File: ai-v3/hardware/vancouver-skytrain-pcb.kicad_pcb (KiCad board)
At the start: 2 copper layers, 200 x 109 mm, 90 parts, among them SW1 TS-1187A-B-A-B, SW2 TS-1187A-B-A-B, SW3 TS-1187A-B-A-B, SW4 TS-1187A-B-A-B, U1 XIAO-RP2040-DIP

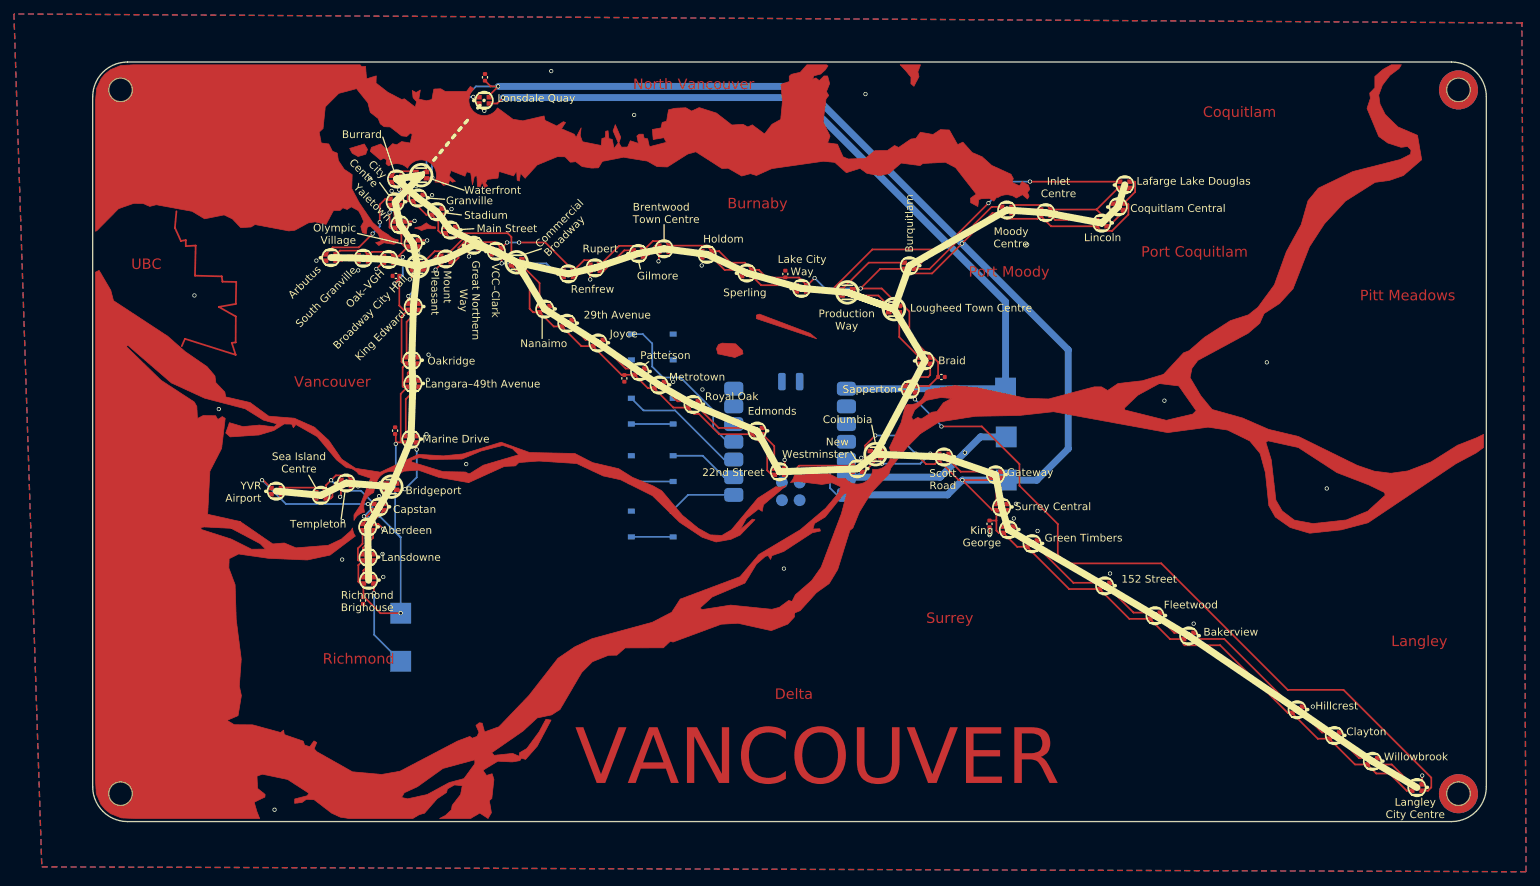
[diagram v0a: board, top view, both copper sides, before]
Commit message: ai-v3: JLCPCB fabrication outputs
hardware/jlcpcb/: gerbers (9 layers, Protel extensions, mask-subtracted
silk) + Excellon drill and map zipped for the order page; BOM and CPL in
JLC's column format for SMT assembly, covering the 68 WS2812B LEDs
(C5349954) and 8 x 10uF 0402 (C52923) - switches are DNP, the XIAO is a
hand-soldered module. tools/make_jlcpcb.py derives the two JLC files
from kicad-cli's raw pos/BOM exports and builds the zip; README.md in
the folder has the upload map and the exact commands.

DRC at this state (KiCad 10.0.5): no unconnected items, no clearance /
edge / courtyard violations; remaining are the two no-net mounting holes
touching the water copper and two thin GND thermals (LED35, LED38).
Includes the user's +5V and GND zone routing fixes.

Co-Authored-By: Claude Fable 5.1 <noreply@anthropic.com>
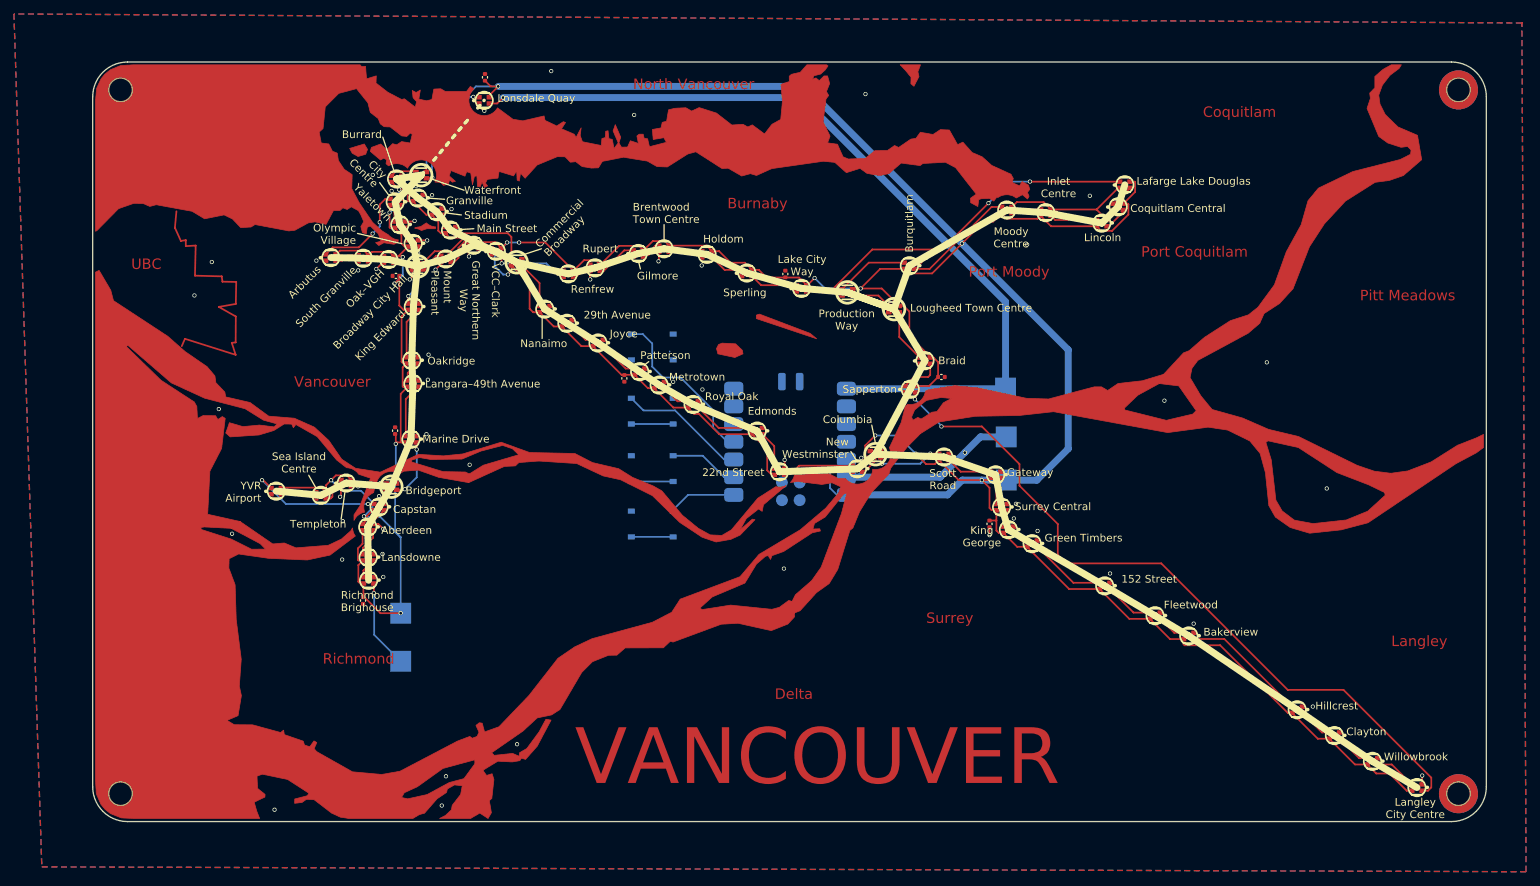
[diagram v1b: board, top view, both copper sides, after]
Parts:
- added ?: LOGO, LOGO, B.Cu at (101.5, 52.1)
- renumbered SW3 to SW2, SW2 to SW3
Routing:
- net +5V: track 643.8 -> 650.7 mm, vias 20 -> 21
- net GND: track 99.7 -> 100.0 mm, vias 54 -> 60
